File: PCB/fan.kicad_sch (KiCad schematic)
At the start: 12 parts, among them M1 P8 Max, U10 TMP468xxRGT, U11 LP5907MFX-3.3

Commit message: Initial commit of project source code
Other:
- moved on the sheet: C12, C13, C14, C15, C16, M1, R6, R7, R8, R9, U10, U11

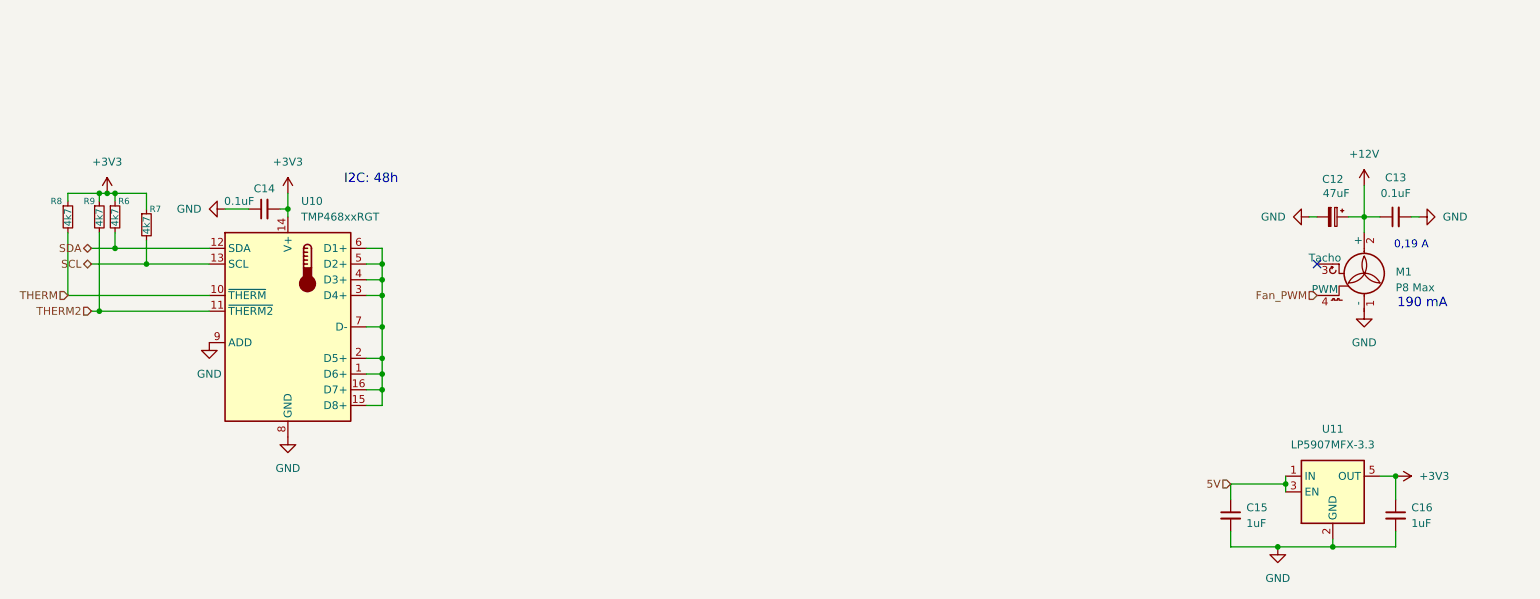
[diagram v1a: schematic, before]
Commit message: updated schematics
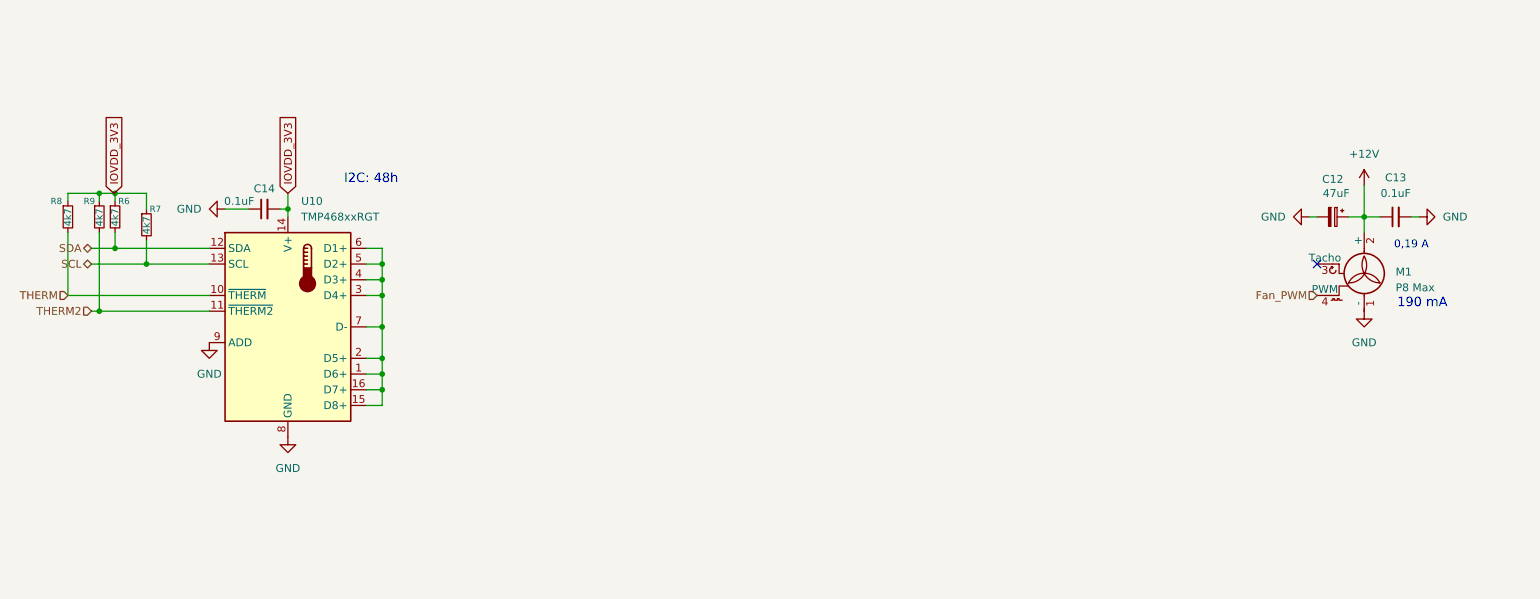
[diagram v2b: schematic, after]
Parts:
- removed C15, C16: 1uF, symbol Device:C_Small
- removed U11: LP5907MFX-3.3, Package_TO_SOT_SMD:SOT-23-5, symbol Regulator_Linear:LP5907MFX-3.3
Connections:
- net +3V3 renamed IOVDD_3V3
